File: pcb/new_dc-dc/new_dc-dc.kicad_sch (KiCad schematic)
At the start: 22 parts, among them J1 power, U1 LMR16030SDDAR

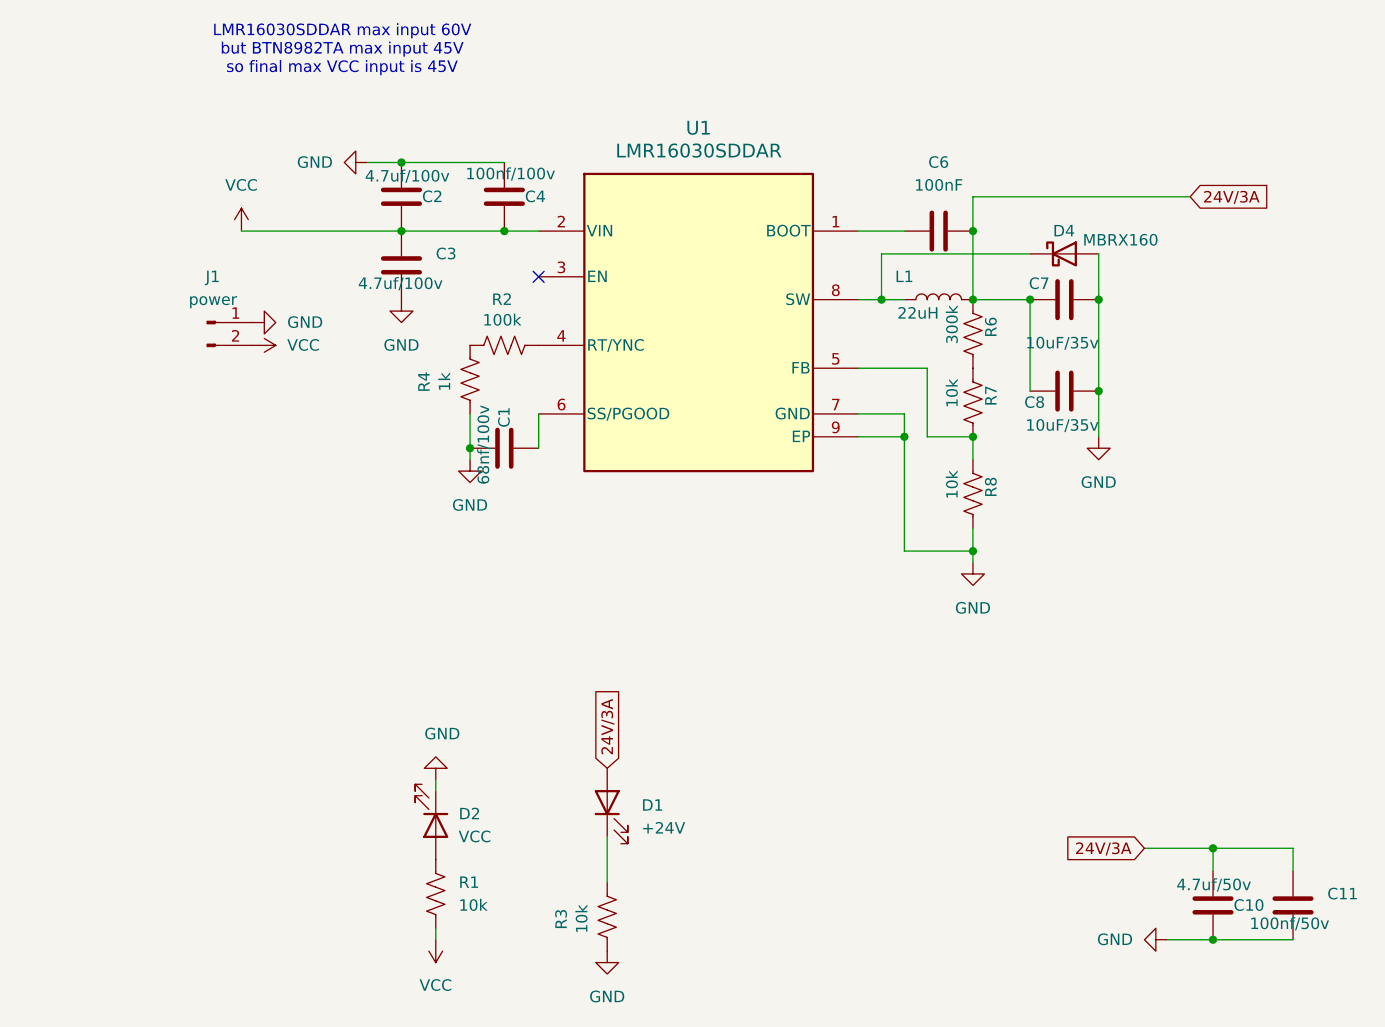
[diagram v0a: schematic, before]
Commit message: feat: new_dc-dc pcb
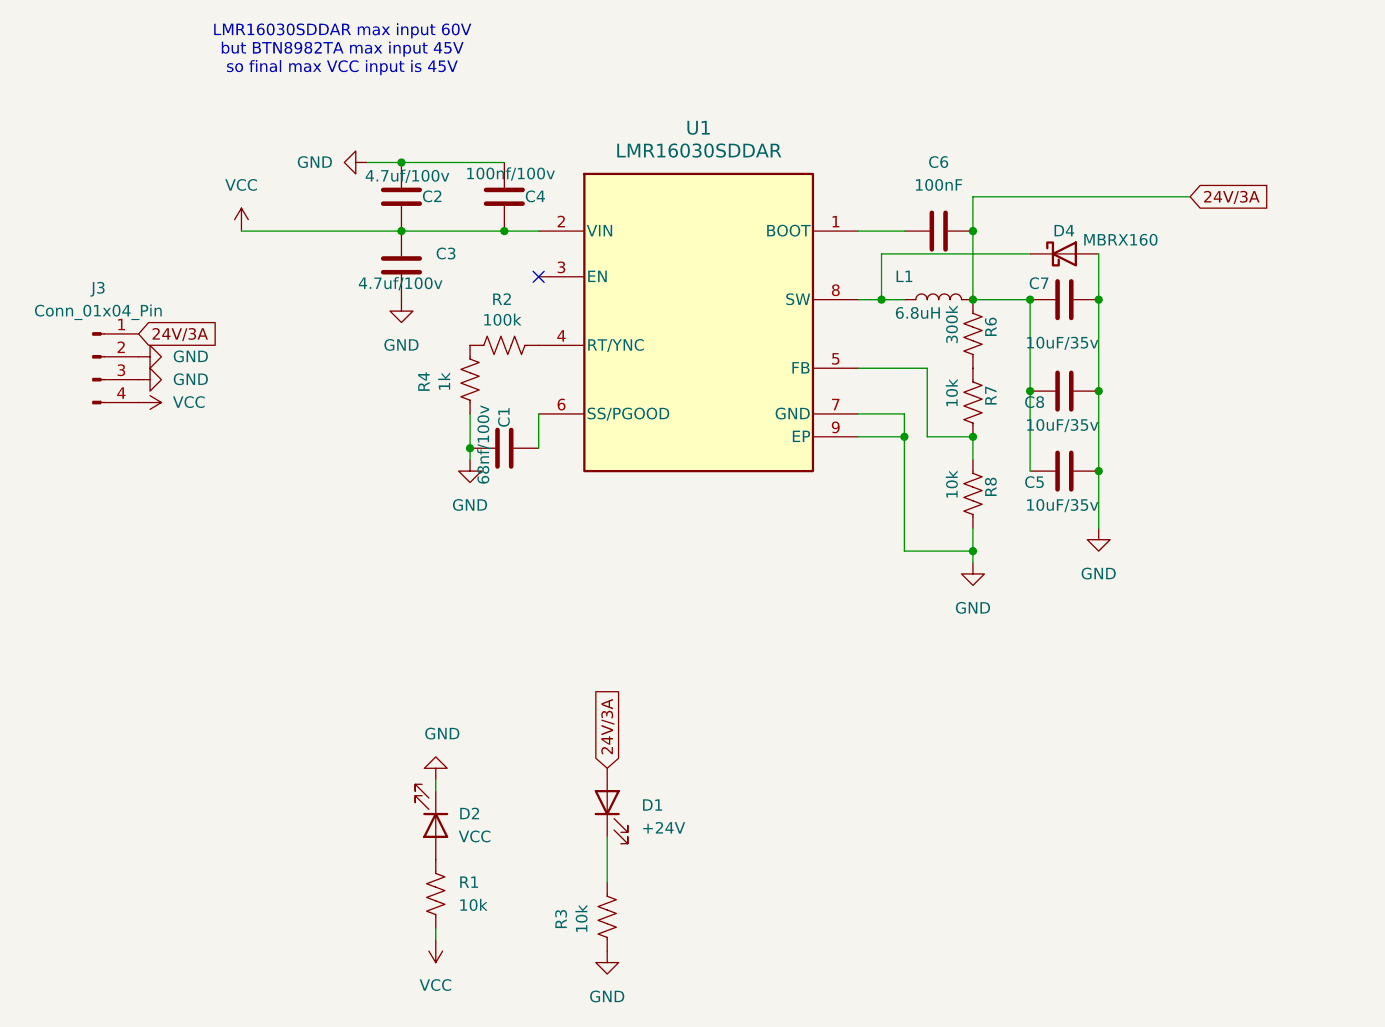
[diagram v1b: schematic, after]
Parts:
- removed C10: 4.7uf/50v, Capacitor_SMD:C_1206_3216Metric, symbol Device:C
- removed C11: 100nf/50v, Capacitor_SMD:C_0603_1608Metric, symbol Device:C
- removed J1: power, Connector_PinHeader_2.54mm:PinHeader_1x02_P2.54mm_Vertical, symbol Connector:Conn_01x02_Pin
- added C5: 10uF/35v, Capacitor_SMD:C_1210_3225Metric, symbol Device:C
- added J3: Conn_01x04_Pin, symbol Connector:Conn_01x04_Pin
- L1: value 22uH -> 6.8uH; footprint Inductor_SMD:L_TDK_SLF12565 -> Inductor_SMD:L_Chilisin_BMRA00040420
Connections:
- net 24V/3A: now also C5.2, J3.1 (Pin_1)
- net GND: now also C5.1, J3.2 (Pin_2), J3.3 (Pin_3)
- net VCC: now also J3.4 (Pin_4)
